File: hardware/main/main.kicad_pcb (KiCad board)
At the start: 4 copper layers, 59.7 x 109.5 mm, 219 parts, among them J101 ST_LINK, J102 USART, J301 Overvoltage_protection, J302 Rad_sensor, J303 Mos_temp, J304 Diode_temp, J601 Supplies, J801 RJ45_Shielded, J802 RJ45_Shielded, Q401 BSC093N15NS5, Q402 BSC093N15NS5, U201 REF3430QDGKRQ1, U202 STM32L431RCTx, U301 INA823DT, U302 INA823DT, U303 INA293A4, U304 INA293A4, U305 TL7726IDR_1, U501 1EDI60N12AF, U601 VXO7805-1000, U602 AMS1117-3.3, U701 MCP2551

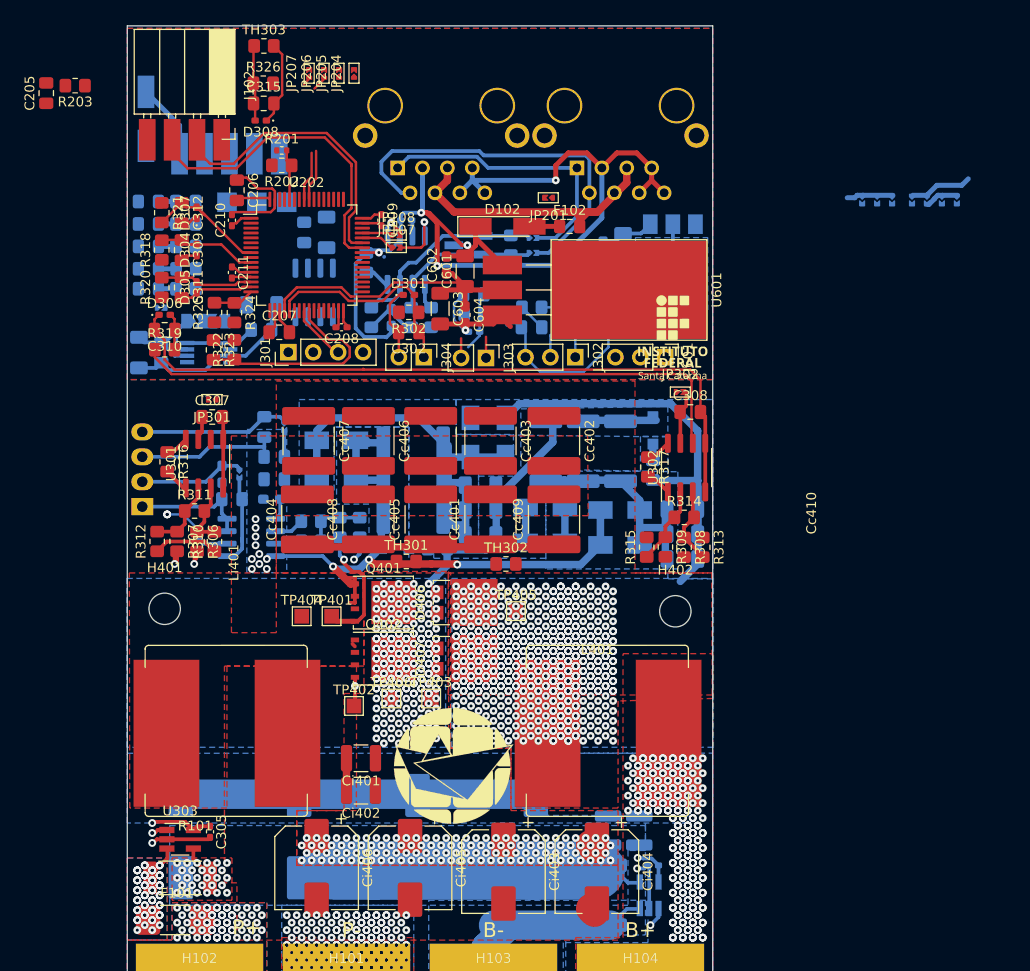
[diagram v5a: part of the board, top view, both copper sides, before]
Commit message: Layout: Control stage routing
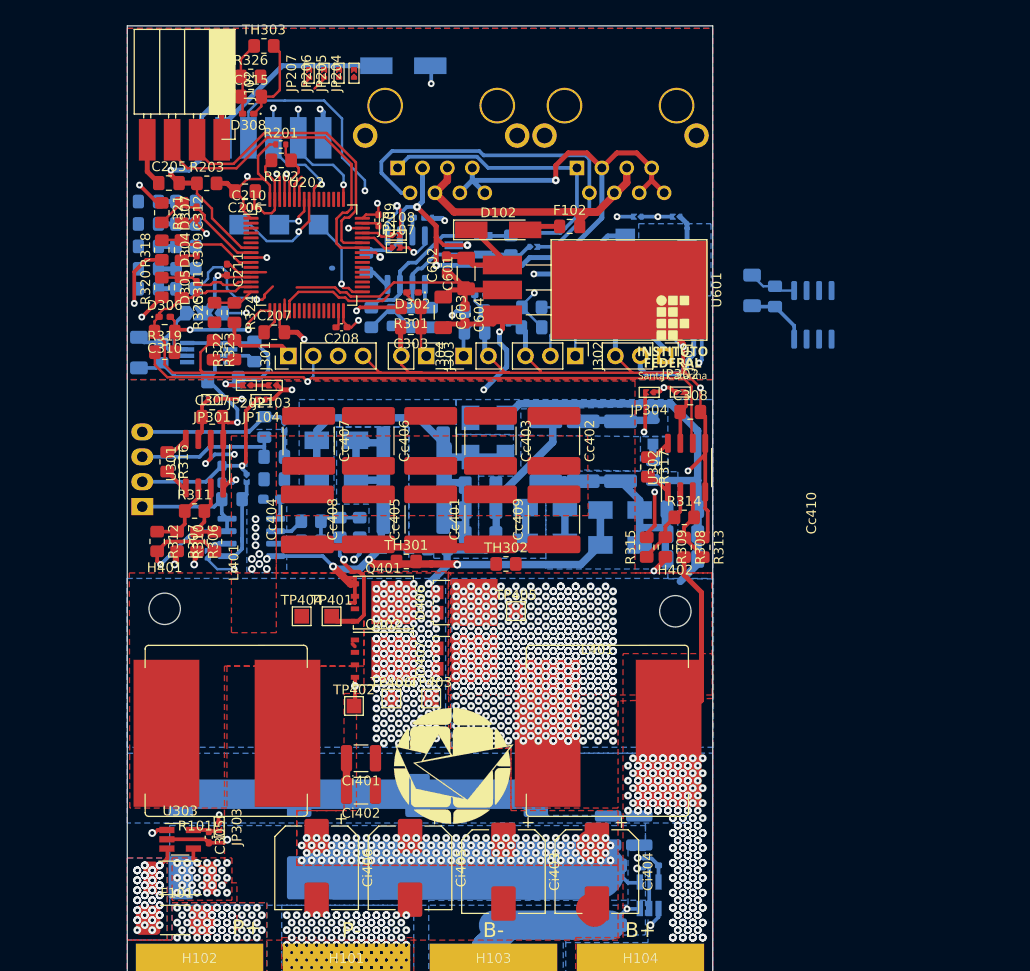
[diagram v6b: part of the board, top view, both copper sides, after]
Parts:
- C302, D301, JP201, R302: moved to B.Cu
- C303, D302, JP103, JP104, JP202, JP303, JP304, R301: moved to F.Cu
- moved JP303 97.5 mm to (28.2, 164.2)
- moved JP104 66.0 mm to (32.4, 120.7), turned to 180 degrees
- moved JP103 66.0 mm to (33.6, 119.2), turned to 180 degrees
- moved U305 50.9 mm to (88.7, 112.0)
- moved C314 48.4 mm to (84.8, 110.1)
- moved JP105 44.4 mm to (49.4, 102.1), turned to 180 degrees
- moved C313 43.8 mm to (82.5, 109.5)
- moved JP304 37.0 mm to (72.0, 119.9), turned to 180 degrees
- moved D101 26.8 mm to (46.9, 86.6), turned to 180 degrees
- moved JP102 25.8 mm to (77.4, 112.1)
- moved JP101 24.1 mm to (74.7, 102.0), turned to 180 degrees
- moved R203 16.7 mm to (26.9, 98.6), turned to 0 degrees
- moved C205 15.5 mm to (23.0, 98.6), turned to 0 degrees
- moved JP202 11.7 mm to (30.9, 119.2), turned to 180 degrees
- moved C605 10.1 mm to (74.1, 112.9), turned to 0 degrees
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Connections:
- R320 pad 1: Net-(R320-Pad1) -> /Analog/I_panel_adc+
- R320 pad 2: /Analog/I_panel_adc+ -> Net-(R320-Pad2)
- U303 pad 1: Net-(R320-Pad1) -> Net-(R320-Pad2)
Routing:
- net /3V3_Analog: track 8.74 -> 150.9 mm, vias 0 -> 6
- net Net-(R321-Pad1): track 2.24 -> 116.6 mm, vias 1 -> 2
- net GND: track 403.5 -> 488.5 mm, vias 9 -> 15
- net /STM32/3V3_MCU: track 11.9 -> 92.6 mm, vias 0 -> 6
- net +5V: track 18.3 -> 87.0 mm, vias 1 -> 5
- net Net-(R320-Pad2): track 0.00 -> 60.3 mm, vias 0 -> 2
- net /Analog/3V3_Ibat: track 4.15 -> 53.9 mm, vias 1 -> 2
- net /PWM: track 0.00 -> 43.2 mm, vias 0 -> 2
- net /B-: track 27.4 -> 68.0 mm, vias 0 -> 2
- net /3V3_STM: track 0.00 -> 34.2 mm, vias 0 -> 2
- net Net-(R318-Pad1): track 0.00 -> 32.5 mm, vias 0 -> 3
- net /STM32/SWDIO: track 0.00 -> 27.7 mm, vias 0 -> 2
- net /STM32/RESET: track 0.00 -> 26.8 mm, vias 0 -> 2
- net /Analog/V_temp_amb: track 7.71 -> 30.2 mm, vias 0 -> 2
- net /B+: track 36.2 -> 56.3 mm
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
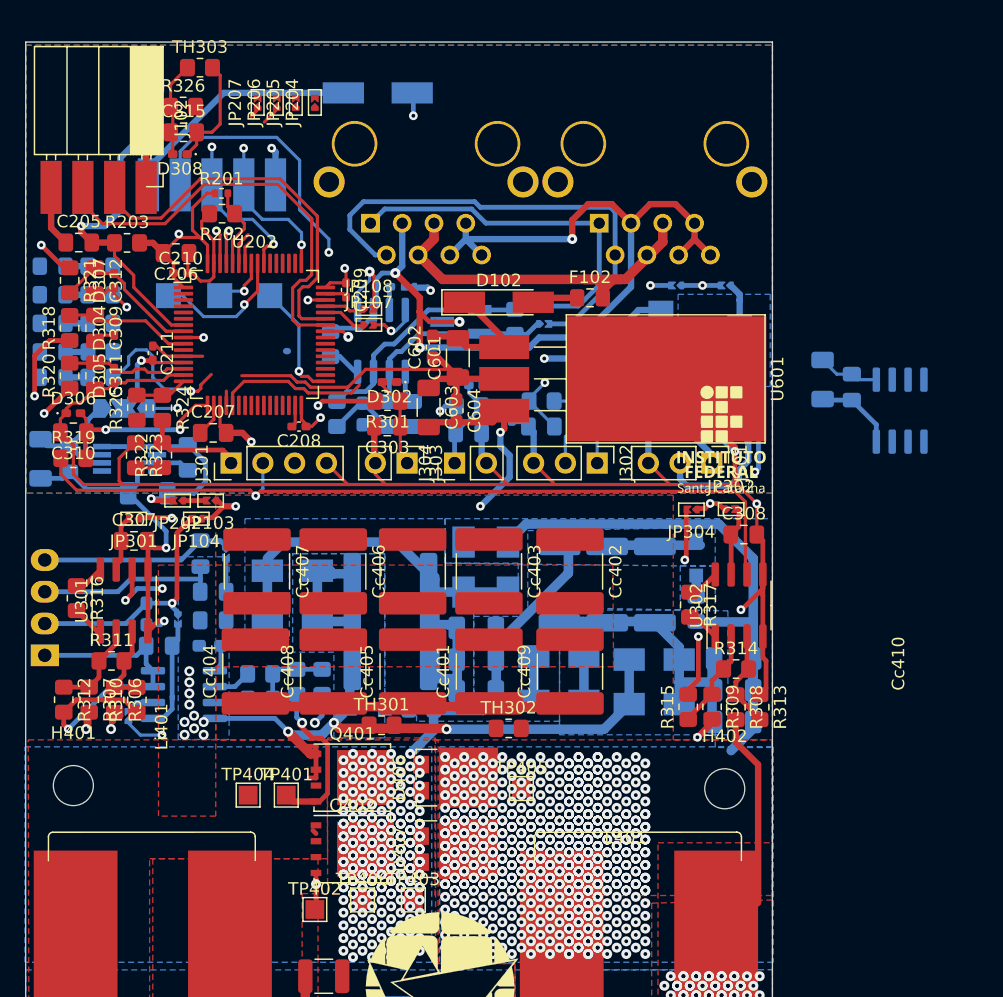
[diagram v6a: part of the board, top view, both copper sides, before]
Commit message: Layout: Nearly complete control stage routing
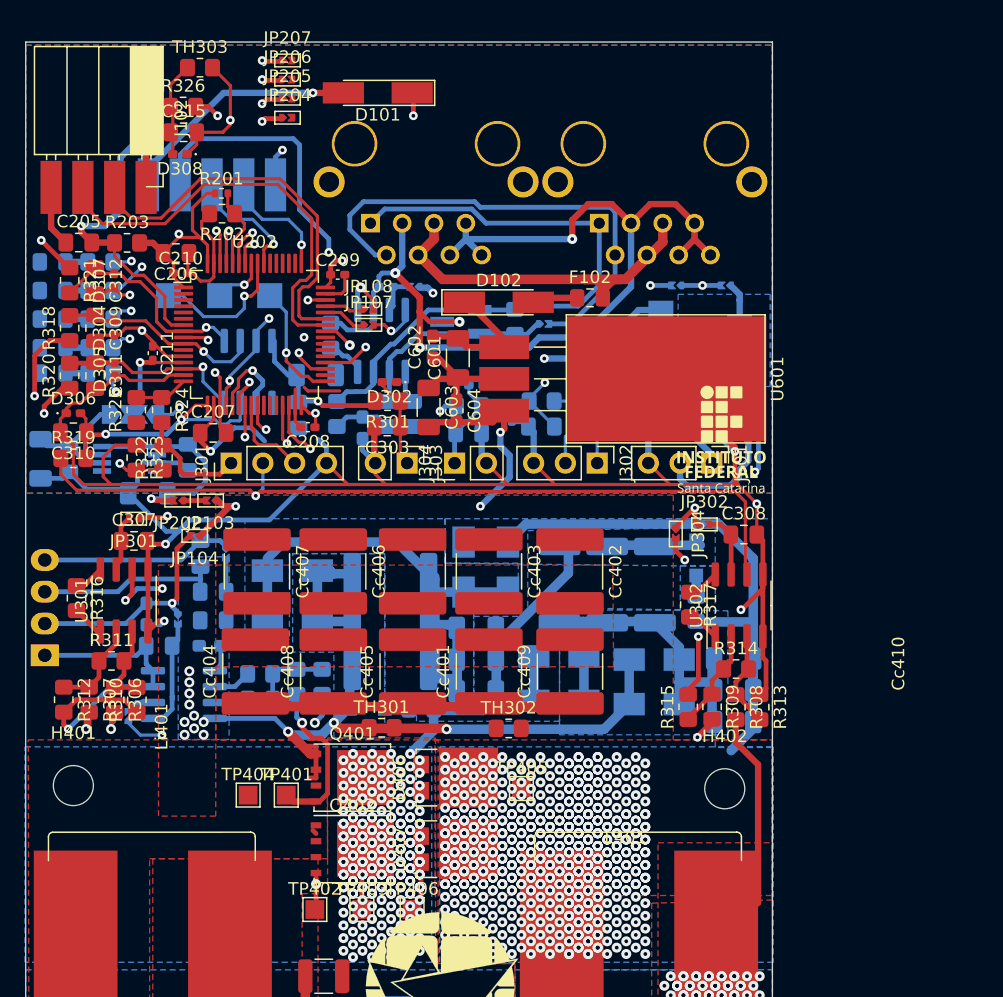
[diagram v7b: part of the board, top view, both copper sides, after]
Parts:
- D101: moved to F.Cu
- moved U305 52.2 mm to (36.6, 108.9), turned to 90 degrees
- moved C314 44.3 mm to (40.6, 112.4), turned to -90 degrees
- moved C313 40.5 mm to (42.0, 109.2), turned to 0 degrees
- moved TP403 4.18 mm to (45.7, 151.9)
- moved JP207 4.12 mm to (39.7, 84.0), turned to 0 degrees
- moved TP406 4.04 mm to (49.7, 151.9)
- moved JP204 2.50 mm to (39.7, 88.6), turned to 0 degrees
- moved JP302 2.46 mm to (73.1, 121.1)
- moved JP304 2.32 mm to (70.8, 121.9), turned to -90 degrees
- moved JP206 2.02 mm to (39.7, 85.5), turned to 0 degrees
- moved C209 1.39 mm to (43.7, 101.1), turned to 0 degrees
- moved JP104 1.38 mm to (32.3, 122.0)
- moved C702 1.11 mm to (45.7, 113.4)
- moved JP203 0.86 mm to (27.4, 112.3)
- moved JP205 0.73 mm to (39.7, 87.1), turned to 0 degrees
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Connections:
- R204 pad 1: Net-(R204-Pad1) -> Net-(U202-Pad29)
- R205 pad 1: Net-(R205-Pad1) -> Net-(U202-Pad30)
- R206 pad 1: Net-(R206-Pad1) -> Net-(U202-Pad35)
- R207 pad 1: Net-(R207-Pad1) -> Net-(U202-Pad36)
- R320 pad 1: /Analog/I_panel_adc+ -> Net-(R320-Pad1)
- R320 pad 2: Net-(R320-Pad2) -> /Analog/I_panel_adc+
- U202 pad 29: Net-(R207-Pad1) -> Net-(U202-Pad29)
- U202 pad 30: Net-(R206-Pad1) -> Net-(U202-Pad30)
- U202 pad 35: Net-(R205-Pad1) -> Net-(U202-Pad35)
- U202 pad 36: Net-(R204-Pad1) -> Net-(U202-Pad36)
- U303 pad 1: Net-(R320-Pad2) -> Net-(R320-Pad1)
- U305 pad 2: /Analog/V_panel_adc+ -> /Analog/V_temp_diode
- U305 pad 6: /Analog/V_temp_diode -> /Analog/V_panel_adc+
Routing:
- net Net-(R320-Pad1): track 0.00 -> 61.4 mm, vias 0 -> 2
- net Net-(R320-Pad2): track 60.3 -> 0.00 mm, vias 2 -> 0
- net /3V3_Analog: track 150.9 -> 194.7 mm, vias 6 -> 7
- net /Analog/V_Rad: track 6.43 -> 42.7 mm, vias 1 -> 2
- net GND: track 488.5 -> 524.5 mm, vias 15 -> 19
- net Net-(U202-Pad36): track 0.00 -> 34.2 mm, vias 0 -> 2
- net /Analog/V_temp_mos: track 10.3 -> 37.5 mm, vias 0 -> 2
- net Net-(U202-Pad35): track 0.00 -> 27.2 mm, vias 0 -> 2
- net Net-(U202-Pad30): track 0.00 -> 26.4 mm, vias 0 -> 2
- net /Analog/V_temp_diode: track 19.9 -> 43.7 mm, vias 0 -> 1
- net Net-(U202-Pad29): track 0.00 -> 23.1 mm, vias 0 -> 2
- net Net-(JP207-Pad1): track 3.59 -> 21.6 mm, vias 1 -> 2
- net /Analog/Vbat_comp_EXT: track 2.14 -> 19.1 mm, vias 0 -> 2
- net Net-(JP206-Pad1): track 4.20 -> 17.4 mm, vias 1 -> 2
- net Net-(JP205-Pad1): track 2.61 -> 15.3 mm, vias 0 -> 2
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
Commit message: Layout: WIP updating control
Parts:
- removed JP202: Enable Voltage Reference, Zenite:SolderJumper-2_P0.5mm_Open_TrianglePad0.5x0.5mm
- moved JP302 0.82 mm to (73.0, 121.9), turned to -90 degrees
- moved JP304 0.69 mm to (71.5, 121.9)
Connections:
- C201 pad 2: /STM32/5VA -> /5V_STM
- C202 pad 2: /STM32/5VA -> /5V_STM
- U201 pad 1: /STM32/5VA -> /5V_STM
- U201 pad 8: /STM32/5VA -> /5V_STM
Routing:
- net Net-(R321-Pad1): track 117.1 -> 27.1 mm
- net /B+: track 56.3 -> 81.0 mm, vias 259 -> 260
- net /5V_STM: track 1.76 -> 19.8 mm, vias 0 -> 1
- net /STM32/5VA: track 17.2 -> 0.00 mm, vias 1 -> 0
- net /B-: track 68.0 -> 66.3 mm
